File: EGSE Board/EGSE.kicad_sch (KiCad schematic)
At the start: 28 parts, among them U1 VOR2121A8, U2 VOR2121A8, U3 INA238AQDGSRQ1, U4 INA238AQDGSRQ1, U5 INA238AQDGSRQ1

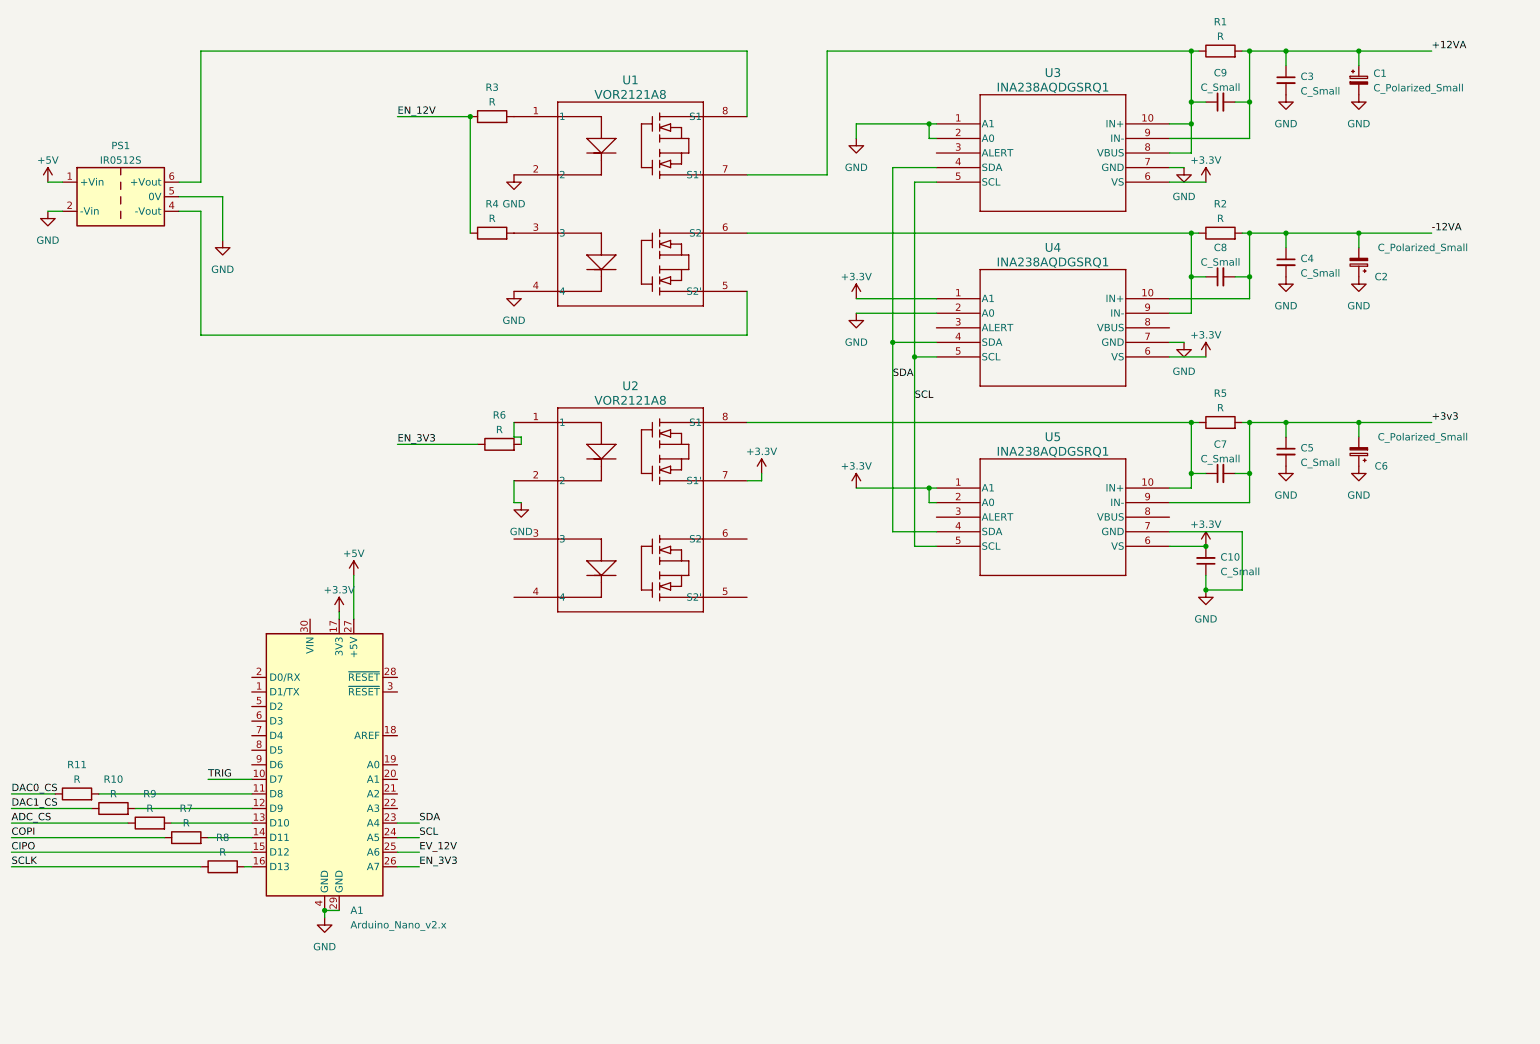
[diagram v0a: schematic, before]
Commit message: Split Sheets
Added sheet to cover Power supplies and monitoring
Modified design to have monitor for -12VA supply running of -12V line with isolated I2C but
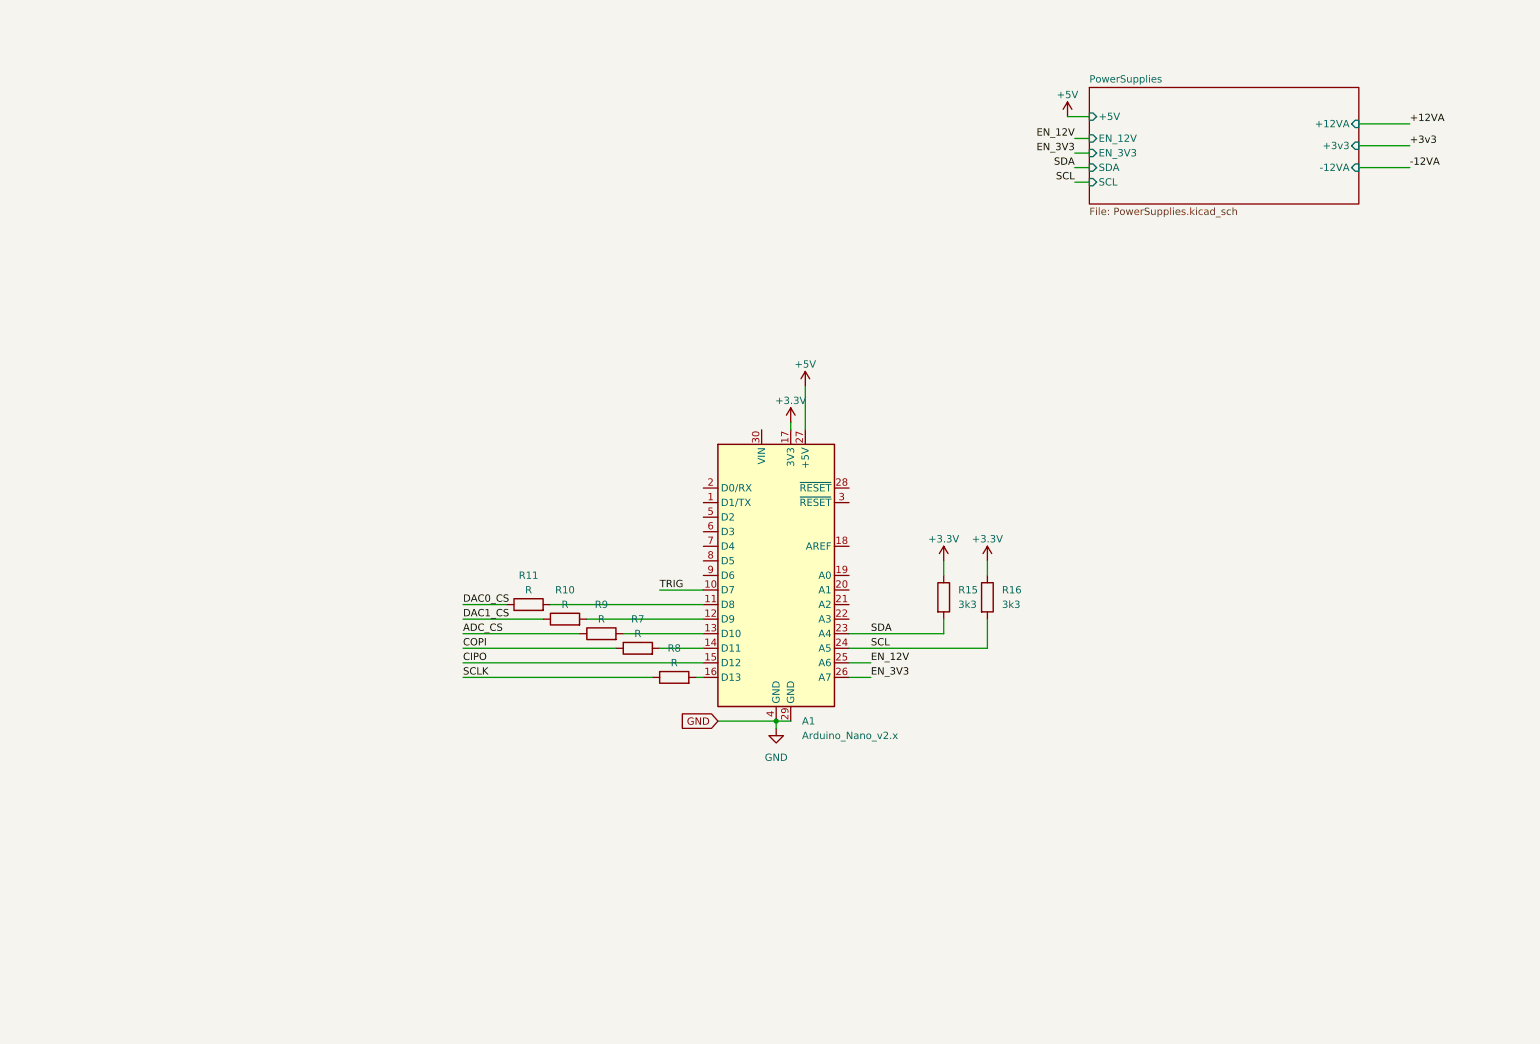
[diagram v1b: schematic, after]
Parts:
- removed C1, C2, C6: C_Polarized_Small, symbol Device:C_Polarized_Small
- removed C10, C3, C4, C5, C7, C8, C9: C_Small, symbol Device:C_Small
- removed PS1: IR0512S, Converter_DCDC:Converter_DCDC_XP_POWER-IAxxxxD_THT, symbol Converter_DCDC:IR0512S
- removed R1, R2, R3, R4, R5, R6: R, symbol Device:R
- removed U1, U2: VOR2121A8, Package_DIP:DIP-8_W7.62mm, symbol Relay_SolidState:VOR2121A8
- removed U3, U4, U5: INA238AQDGSRQ1, Package_SO:VSSOP-10_3x3mm_P0.5mm, symbol Power_Management:INA238AQDGSRQ1
- added R15, R16: 3k3, symbol Device:R
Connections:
- net EV_12V is gone; now on net EN_12V: A1.25 (A6)
- net +3.3V: now also R15.1, R16.1
- net SCL: now also R16.2
- net SDA: now also R15.2
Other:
- added sheet PowerSupplies (PowerSupplies.kicad_sch)
- moved on the sheet: A1, R10, R11, R7, R8, R9

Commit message: EGSE board updates
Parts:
- added J1: DC37_Receptacle, symbol Connector:DC37_Receptacle
- R10, R11, R7, R8, R9: value R -> 33R
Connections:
- net +3v3: now also J1.6
- net RTD_CS: now reaches A1.9 (D6)
- net ADC_CS renamed DETEC_ADC_CS
- net DETEC_ADC_CS: now also J1.20
- net CIPO renamed DETEC_MISO
- net COPI renamed DETEC_MOSI
- net DETEC_MOSI: now also J1.4
- net DAC0_CS renamed SWIR_DAC_CS
- net SWIR_DAC_CS: now also J1.3
- net DAC1_CS renamed MWIR_DAC_CS
- net MWIR_DAC_CS: now also J1.19
- net SCLK renamed DETEC_SCK
- new net DETEC_SCLK: J1.5
- new net DETEC_TRP: J1.1
- new net DETEC_TRP_RTN: J1.17
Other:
- added sheet BoardHeater (HeaterSupply.kicad_sch)
- sheet PowerSupplies ports: added +12_Unswitched, +3V3, -12V_Unswitched, DETEC_+12VA, DETEC_+3v3, DETEC_-12VA; removed +12VA, +3v3, -12VA
- note added: "Arduino Nano ESP32"
- note added: "Power supplies and current monitoring"
- moved on the sheet: A1, R10, R11, R15, R16, R7, R8, R9

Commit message: Change to heater power
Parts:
- added C13, C14, C15: 0.1u, symbol Device:C_Small
- added R12: 4K, symbol Device:R
- added U5: MAX31865xAP, Package_SO:SSOP-20_5.3x7.2mm_P0.65mm, symbol Sensor_Temperature:MAX31865xAP
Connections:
- net +3.3V: now also C13.1, C14.1, U5.2 (DVDD), U5.3 (VDD)
- net DETEC_MISO: now also U5.17 (SDO)
- net DETEC_MOSI: now also U5.14 (SDI)
- net DETEC_SCK: now also U5.15 (SCLK)
- net DETEC_TRP: now also C15.1, U5.10 (RTDIN+), U5.8 (FORCE+)
- net DETEC_TRP_RTN: now also C15.2, U5.11 (RTDIN-), U5.12 (FORCE-)
- net GND: now also C13.2, C14.2, U5.13 (GND), U5.18 (DGND), U5.19 (GND), U5.9 (FORCE2)
- new net: R12.1, U5.4 (BIAS), U5.5 (REFIN+)
- new net: R12.2, U5.6 (REFIN-), U5.7 (ISENSOR)
- new net RTD_MON_CS: U5.16 (~{CS})
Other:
- note added: "SPI interface for RTD"

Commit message: Friday updates. PCB first draft
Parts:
- C13, C14, C15: footprint (none) -> Capacitor_SMD:C_0402_1005Metric
- J1: footprint (none) -> Connector_Dsub:DSUB-37_Female_Vertical_P2.77x2.84mm_MountingHoles
- R10, R11, R12, R15, R16, R7, R8, R9: footprint (none) -> Resistor_SMD:R_0612_1632Metric
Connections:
- net +3v3 is gone; now on net DETEC_+3v3: J1.6
- net DETEC_SCLK is gone; now on net DETEC_SCK: J1.5
- net RTD_CS is gone; now on net RTD_MON_CS: A1.9 (D6)
- net +3.3V: now also R16.2; no longer R16.1
- net DETEC_+12VA: now also J1.12, J1.30
- net DETEC_-12VA: now also J1.16, J1.34
- net DETEC_ADC_CS: now also J1.23; no longer J1.20
- net DETEC_MISO: now also J1.24
- net DETEC_TRP_RTN: now also J1.20; no longer J1.17
- net GND: now also J1.14, J1.25, J1.28, J1.32
- net HTR_DAC_CS: now also A1.7 (D4)
- net HTR_EN: now also A1.8 (D5)
- net MWIR_DAC_CS: now also J1.22; no longer J1.19
- net SCL: now also R16.1; no longer R16.2
- net DETEC_HTR: now reaches J1.8
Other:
- sheet BoardHeater ports: added +12V_HTR; removed +3V3, DETEC_HTR, DETEC_MISO, RTD_MON_CS, SCL, SDA
- sheet PowerSupplies ports: added +12V_HTR, DETEC_HTR; removed +12_Unswitched
- moved on the sheet: J1, R16

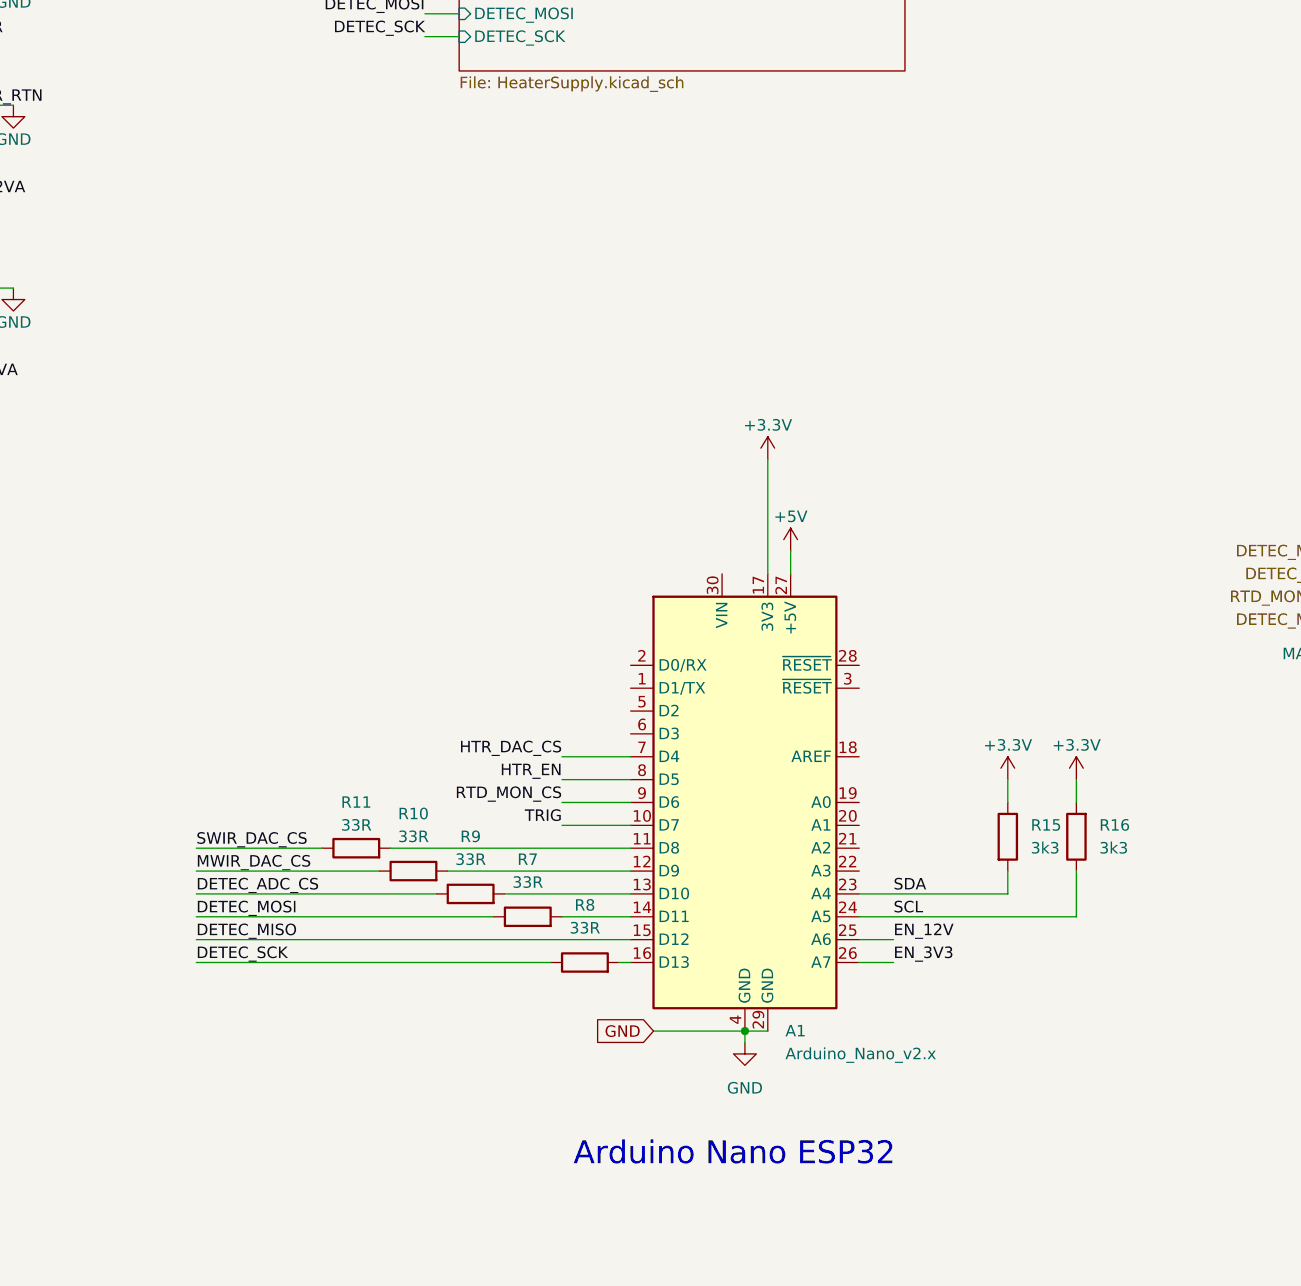
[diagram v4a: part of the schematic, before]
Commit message: Regular update
Created Gerber files for production
Changed names in arduino code to reflect signal names used by MSSL and on EGSE board
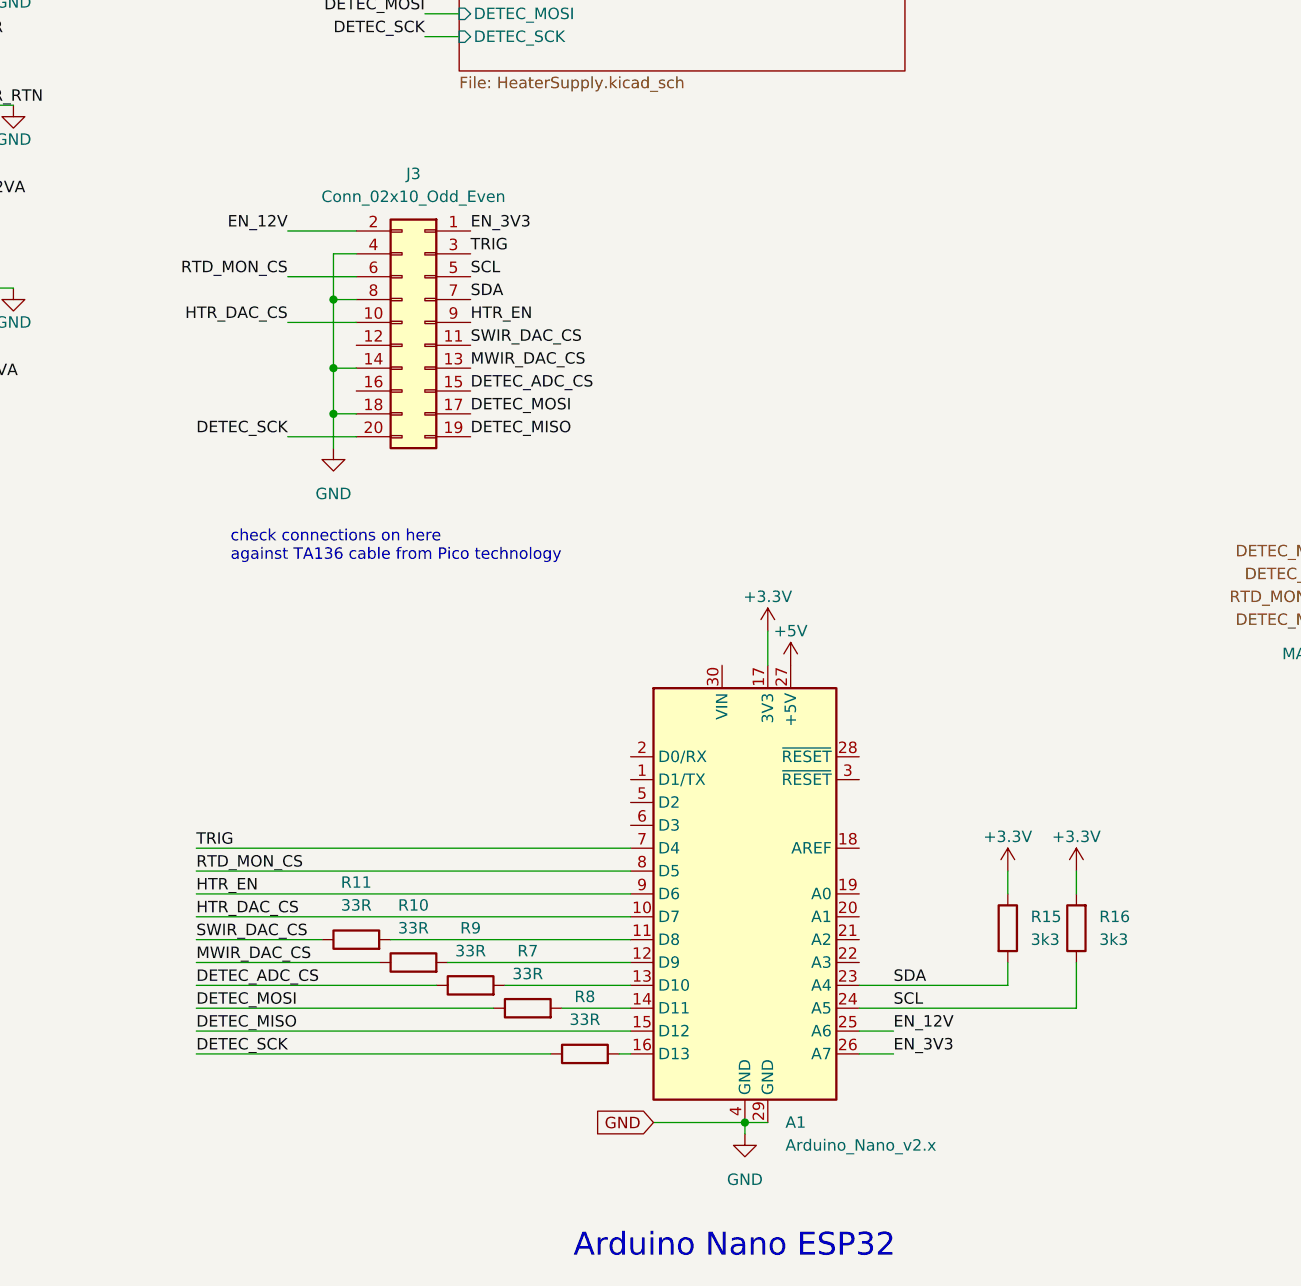
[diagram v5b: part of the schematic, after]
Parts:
- added J3: Conn_02x10_Odd_Even, Connector_PinHeader_2.54mm:PinHeader_2x10_P2.54mm_Vertical, symbol Connector_Generic:Conn_02x10_Odd_Even
- R10, R11, R12, R15, R16, R7, R8, R9: footprint Resistor_SMD:R_0612_1632Metric -> Resistor_SMD:R_0805_2012Metric
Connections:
- net DETEC_ADC_CS: now also J3.15 (Pin_15)
- net DETEC_MISO: now also J3.19 (Pin_19)
- net DETEC_MOSI: now also J3.17 (Pin_17)
- net DETEC_SCK: now also J3.20 (Pin_20)
- net EN_12V: now also J3.2 (Pin_2)
- net EN_3V3: now also J3.1 (Pin_1)
- net GND: now also J3.14 (Pin_14), J3.18 (Pin_18), J3.4 (Pin_4), J3.8 (Pin_8)
- net HTR_DAC_CS: now also A1.10 (D7), J3.10 (Pin_10); no longer A1.7 (D4)
- net HTR_EN: now also A1.9 (D6), J3.9 (Pin_9); no longer A1.8 (D5)
- net MWIR_DAC_CS: now also J3.13 (Pin_13)
- net RTD_MON_CS: now also A1.8 (D5), J3.6 (Pin_6); no longer A1.9 (D6)
- net SCL: now also J3.5 (Pin_5)
- net SDA: now also J3.7 (Pin_7)
- net SWIR_DAC_CS: now also J3.11 (Pin_11)
- net TRIG: now also A1.7 (D4), J3.3 (Pin_3); no longer A1.10 (D7)
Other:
- note added: "check connections on here against TA136 cable from Pico technology"
- moved on the sheet: A1, R10, R11, R15, R16, R7, R8, R9
